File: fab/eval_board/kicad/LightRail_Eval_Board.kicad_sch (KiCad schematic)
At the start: 0 parts

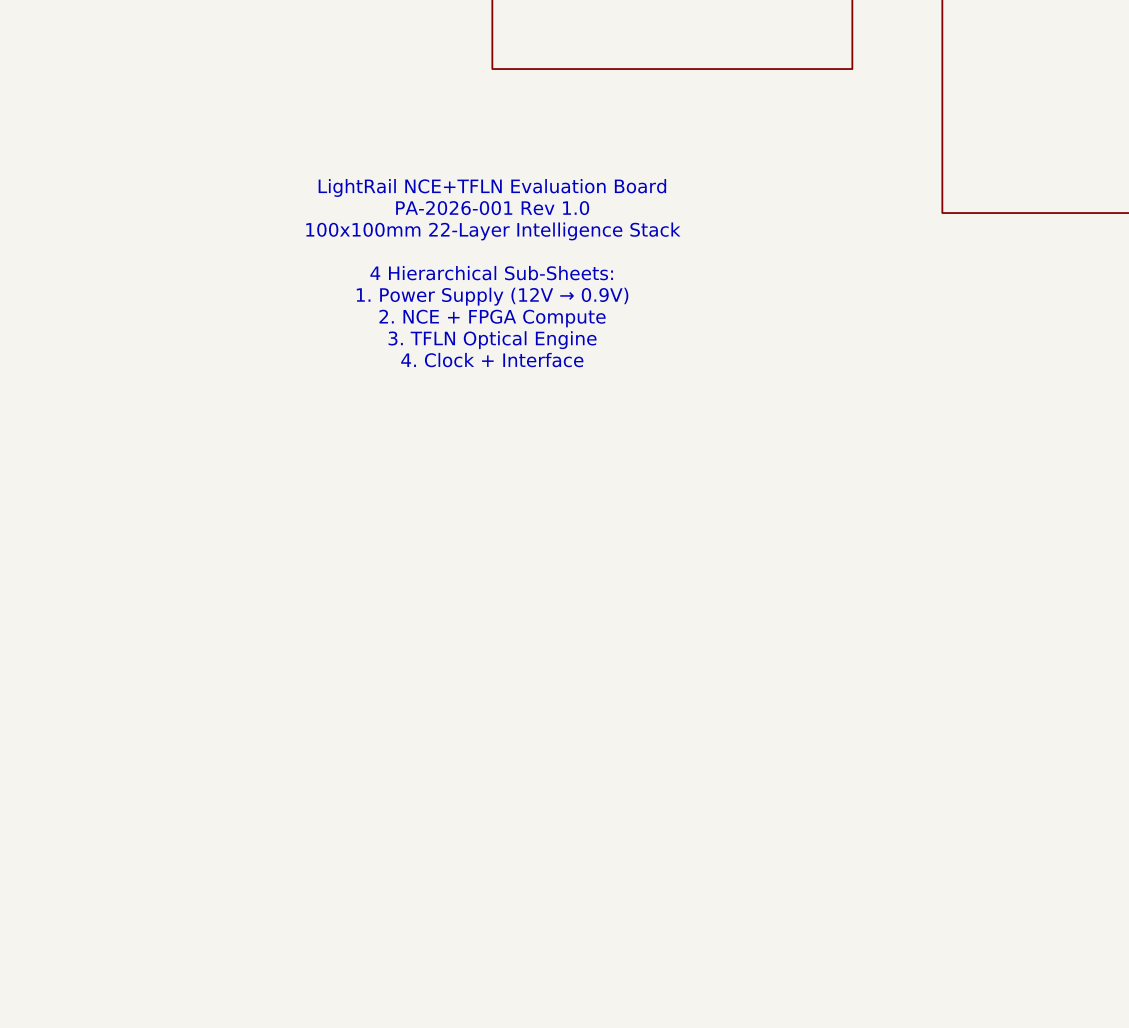
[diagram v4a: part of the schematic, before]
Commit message: feat: add Sierra Circuits 17-point schematic checklist + fix guidelines 6 & 8
- Add revision history table to top-level schematic (guideline 6)
- Add block diagram with signal flow to top-level schematic (guideline 8)
- Add table of contents with page references
- Create comprehensive 17-point checklist report: 17/17 PASS

Co-Authored-By: Bola Olatunji <bola.olatunji@ai.lightos.sh>
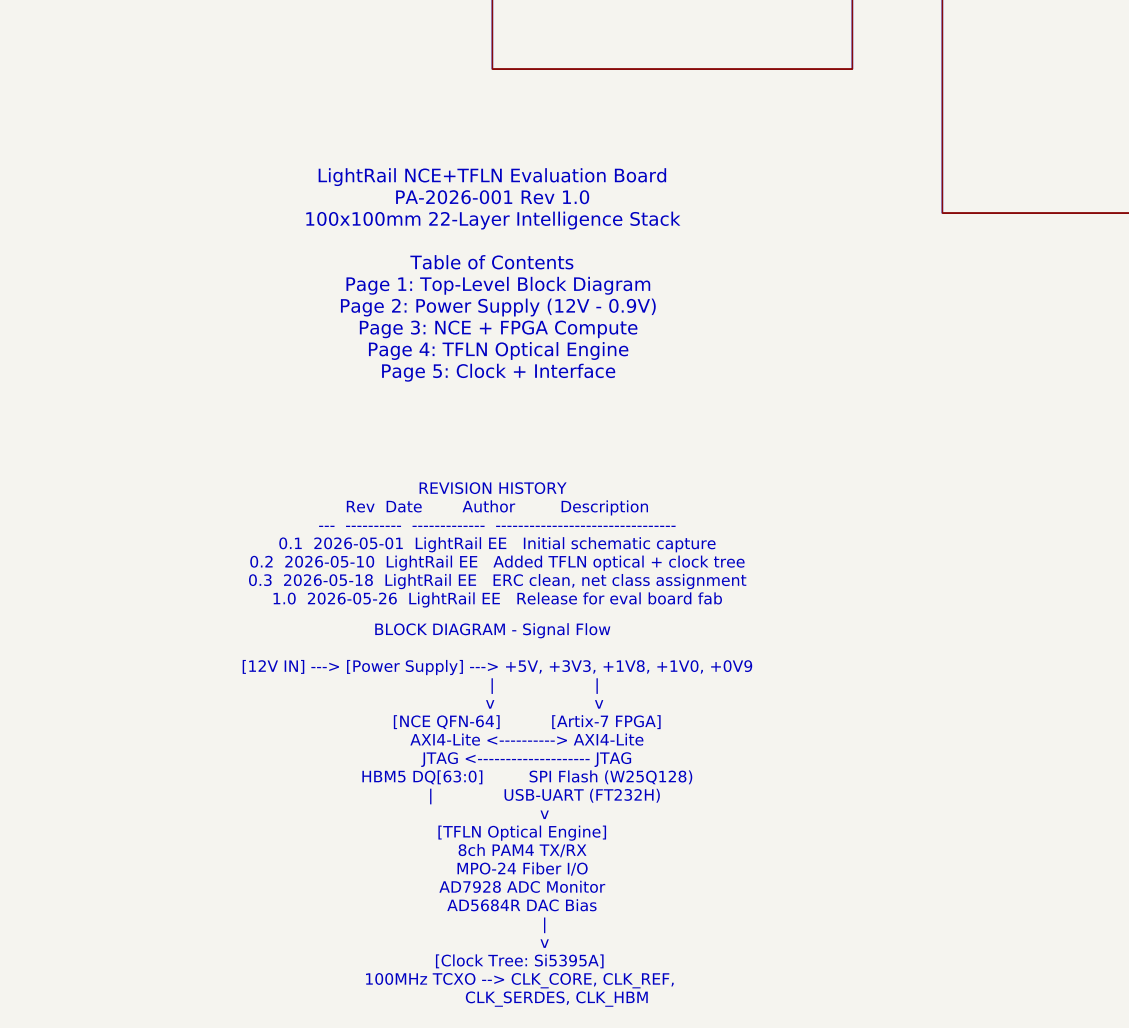
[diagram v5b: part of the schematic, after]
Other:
- note added: "BLOCK DIAGRAM - Signal Flow [12V IN] ---> [Power Supply] ---> +5V, +3V3, +1V8, +1V0, +0V9 | | v v [NCE QFN-64] [Artix-7 FPGA] AXI4-Lite <----------> AXI4-Lite JTAG <-------------------- JTAG HBM5 DQ[63:0] SPI Flash (W25Q128) | USB-UART (FT232H) v [TFLN Optical Engine] 8ch PAM4 TX/RX MPO-24 Fiber I/O AD7928 ADC Monitor AD5684R DAC Bias | v [Clock Tree: Si5395A] 100MHz TCXO --> CLK_CORE, CLK_REF, C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"
- note added: "LightRail NCE+TFLN Evaluation Board PA-2026-001 Rev 1.0 100x100mm 22-Layer Intelligence Stack Table of Contents Page 1: Top-Level Block Diagram Page 2: Power Supply (12V - 0.9V) Page 3: NCE + FPGA Compute Page 4: TFLN Optical Engine Page 5: Clock + Interface"
- note added: "REVISION HISTORY Rev Date Author Description --- ---------- ------------- -------------------------------- 0.1 2026-05-01 LightRail EE Initial schematic capture 0.2 2026-05-10 LightRail EE Added TFLN optical + clock tree 0.3 2026-05-18 LightRail EE ERC clean, net class assignment 1.0 2026-05-26 LightRail EE Release for eval board fab"
- note removed: "LightRail NCE+TFLN Evaluation Board PA-2026-001 Rev 1.0 100x100mm 22-Layer Intelligence Stack 4 Hierarchical Sub-Sheets: 1. Power Supply (12V → 0.9V) 2. NCE + FPGA Compute 3. TFLN Optical Engine 4. Clock + Interface"
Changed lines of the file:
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@@
 		(property "Sheetfile" "sheets/clock_interface.kicad_sch" (at 190.00 63.27 0) (effects (font (size 1.27 1.27)) (hide yes)))
 	)
-	(text "LightRail NCE+TFLN Evaluation Board\nPA-2026-001 Rev 1.0\n100x100mm 22-Layer Intelligence Stack\n\n4 Hierarchical Sub-Sheets:\n1. Power Supply (12V → 0.9V)\n2. NCE + FPGA Compute\n3. TFLN Optical Engine\n4. Clock + Interface" (at 30.00 75.00 0) (effects (font (size 1.50 1.50))))
+	(text "LightRail NCE+TFLN Evaluation Board\nPA-2026-001 Rev 1.0\n100x100mm 22-Layer Intelligence Stack\n\nTable of Contents\n  Page 1: Top-Level Block Diagram\n  Page 2: Power Supply (12V - 0.9V)\n  Page 3: NCE + FPGA Compute\n  Page 4: TFLN Optical Engine\n  Page 5: Clock + Interface" (at 30.00 75.00 0) (effects (font (size 1.50 1.50))))
+	(text "REVISION HISTORY\n  Rev  Date        Author         Description\n  ---  ----------  -------------  --------------------------------\n  0.1  2026-05-01  LightRail EE   Initial schematic capture\n  0.2  2026-05-10  LightRail EE   Added TFLN optical + clock tree\n  0.3  2026-05-18  LightRail EE   ERC clean, net class assignment\n  1.0  2026-05-26  LightRail EE   Release for eval board fab" (at 30.00 105.00 0) (effects (font (size 1.27 1.27))))
+	(text "BLOCK DIAGRAM - Signal Flow\n\n  [12V IN] ---> [Power Supply] ---> +5V, +3V3, +1V8, +1V0, +0V9\n                     |                    |\n                     v                    v\n              [NCE QFN-64]          [Artix-7 FPGA]\n              AXI4-Lite <----------> AXI4-Lite\n              JTAG <-------------------- JTAG\n              HBM5 DQ[63:0]         SPI Flash (W25Q128)\n                     |              USB-UART (FT232H)\n                     v\n            [TFLN Optical Engine]\n            8ch PAM4 TX/RX\n            MPO-24 Fiber I/O\n            AD7928 ADC Monitor\n            AD5684R DAC Bias\n                     |\n                     v\n           [Clock Tree: Si5395A]\n           100MHz TCXO --> CLK_CORE, CLK_REF,\n                          CLK_SERDES, CLK_HBM" (at 30.00 135.00 0) (effects (font (size 1.27 1.27))))
 	(sheet_instances
 		(path "/" (page "1"))
